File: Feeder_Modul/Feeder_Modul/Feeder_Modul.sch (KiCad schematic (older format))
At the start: 68 parts, among them J101 Conn_02x01, J102 Conn_01x06_Male, J103 Conn_02x01, J104 Conn_01x02_Male, J105 Conn_01x02_Male, J106 USB_A, J107 Conn_02x07_Odd_Even, Q101 BC847, SW101 SW_Push, SW102 SW_Push, SW103 SW_Push, SW104 SW_Push, SW105 SW_Push, U101 TPS560430, U102 STM32F105R8Tx, U103 SN65HVD230DR, U104 EE-SX1350_PCB, U105 DRV8835, Y101 48MHz

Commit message: PCB fast fertig geroutet, I2C EEPROM hinzugefügt
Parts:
- removed U103: SN65HVD230DR, Package_SO:SOIC-8_3.9x4.9mm_P1.27mm, symbol Interface_CAN_LIN:TJA1051T-3
- added C1: 100n 50V, Capacitor_SMD:C_0603_1608Metric, symbol Device:C_Small
- added C124, C2, C3: 10u 50V, Capacitor_SMD:C_1210_3225Metric, symbol Device:C_Small
- added D103, D104: LED_Blue, LED_SMD:LED_0603_1608Metric, symbol Device:LED_Small
- added J1, J108: Conn_02x01, Connector_PinHeader_2.54mm:PinHeader_1x02_P2.54mm_Vertical, symbol Connector_Generic:Conn_02x01
- added L1: 12u SRN4018, Inductor_SMD:L_Bourns-SRN4018, symbol Device:L_Small
- added R1, R2: 51K, Resistor_SMD:R_0603_1608Metric, symbol Device:R_Small
- added R123, R124, R126: 1k, Resistor_SMD:R_0603_1608Metric, symbol Device:R_Small
- added R125: DNP, Resistor_SMD:R_0603_1608Metric, symbol Device:R_Small
- added R127, R129: 10K, Resistor_SMD:R_0603_1608Metric, symbol Device:R_Small
- added R3: 22K1, Resistor_SMD:R_0603_1608Metric, symbol Device:R_Small
- added R4: 88K7, Resistor_SMD:R_0603_1608Metric, symbol Device:R_Small
- added U1: TPS560430, Package_TO_SOT_SMD:SOT-23-6, symbol PorjectLibrary:TPS560430
- added U103: M24C01-WMN, Package_SO:SOIC-8_3.9x4.9mm_P1.27mm, symbol Memory_EEPROM:M24C01-WMN
- added U107: SN65HVD230, Package_SO:SOIC-8_3.9x4.9mm_P1.27mm, symbol Interface_CAN_LIN:SN65HVD230
- C103: value 100n 50V -> 10u 50V; footprint Capacitor_SMD:C_0603_1608Metric -> Capacitor_SMD:C_1210_3225Metric; LCSC C282519 -> C1849
- C116, C119: value 100n -> 100n 50V; LCSC C83060 -> C282519
- C121: value 10u -> 10u 50V
- D101: value LED_Small -> LED_red; LCSC (none) -> C118330
- D102: value LED_Small -> LED_green; LCSC (none) -> C205443
- J101, J103: LCSC (none) -> C358684
- J104, J105: value Conn_01x02_Male -> Conn_02x01; LCSC (none) -> C358684
- J106: footprint Connector_USB:USB_A_CNCTech_1001-011-01101_Horizontal -> ProjectFootprints:USB-A-Conn_LCSC; symbol Connector:USB_A -> Feeder_Modul-rescue:USB_A-Connector; LCSC (none) -> C46405
- R108: value 10K -> 1k; LCSC C99198 -> C21190
- R109, R115, R121, R122: LCSC (none) -> C21190
- R113, R116, R117, R118, R119, R120: value 10k -> 10K; LCSC (none) -> C99198
- U102: LCSC (none) -> C80986
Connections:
- net labels added: ADDR0, ADDR1, ADDR2, ADDR3, ADDR4, ADDR5, ADDR6, ADDR7, I2C1_SCL, I2C1_SDA, PA5, PA6, PA7, PA8, PB12, PB13, PB14, PB15, PC4, PC5, PC6, PC7, PC8, PC9, TIM3_CH1, TIM3_CH2
- net labels removed: AD0, AD1, AD2, AD3, AD4, AD5, AD6, AD7, PA11, PA12, VBUS, VBUS_EN
- wire segments 218 -> 295
- no-connect marks 3 -> 29
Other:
- note added: "Address:\n0x50"
- note added: "Built in ESD Protection 16kV"
- note added: "High Speed Mode"
- note added: "Write enabled\n"
- note removed: "Replacement\nTJA1051T-3"
- moved on the sheet: C119, C121, J107, L102, R110, R111, R114

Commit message: Feeder fertig
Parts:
- added R128, R130, R131, R132, R133, R134, R135, R136: 88K7, Resistor_SMD:R_0603_1608Metric, symbol Device:R_Small
- R112: value 0R -> DNP
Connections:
- net +3V3: now also R128.2, R130.2, R131.2, R132.2, R133.2, R134.2, R135.2, R136.2
- net ADDR0: now also R128.1
- net ADDR1: now also R130.1
- net ADDR2: now also R131.1
- net ADDR3: now also R132.1
- net ADDR4: now also R133.1
- net ADDR5: now also R134.1
- net ADDR6: now also R135.1
- net ADDR7: now also R136.1
- net BTN_SBACK: now also U102.56 (PB4)
- net BTN_SFOR: now also U102.55 (PB3)
- net BTN_TBACK: now also U102.15 (PA1)
- net BTN_TFOR: now also U102.16 (PA2)
- net ENC_OUT: now also U102.30 (PB11)
- no-connect marks 29 -> 24
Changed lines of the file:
@@
 EESchema Schematic File Version 4
-EELAYER 30 0
+LIBS:Feeder_Modul-cache
+EELAYER 26 0
 EELAYER END
 $Descr A3 16535 11693
@@
 AR Path="/6057AAB9" Ref="R112"  Part="1"
 F 0 "R112" V 9600 1900 50  0000 R CNN
-F 1 "0R" V 9800 1850 50  0000 R CNN
+F 1 "DNP" V 9800 1900 50  0000 R CNN
 F 2 "Resistor_SMD:R_0603_1608Metric" H 9700 1850 50  0001 C CNN
 F 3 "~" H 9700 1850 50  0001 C CNN
@@
 NoConn ~ 5250 7650
 NoConn ~ 5250 7750
-NoConn ~ 5250 7850
-NoConn ~ 5250 7950
 NoConn ~ 5250 8050
 NoConn ~ 5250 8550
-NoConn ~ 5250 8650
 NoConn ~ 3850 8650
 NoConn ~ 3850 8750
@@
 NoConn ~ 3850 7350
 NoConn ~ 5250 5850
-NoConn ~ 5250 5950
-NoConn ~ 5250 6050
 NoConn ~ 5250 6150
 NoConn ~ 5250 6250
@@
 Wire Wire Line
 	2100 2500 2950 2500
+Text Label 14150 7300 2    50   ~ 0
+ADDR0
+Text Label 14150 7500 2    50   ~ 0
+ADDR2
+Text Label 14150 7700 2    50   ~ 0
+ADDR4
+Text Label 14150 7900 2    50   ~ 0
+ADDR6
+Text Label 14150 7400 2    50   ~ 0
+ADDR1
+Text Label 14150 7600 2    50   ~ 0
+ADDR3
+Text Label 14150 7800 2    50   ~ 0
+ADDR5
+Text Label 14150 8000 2    50   ~ 0
+ADDR7
+$Comp
+L Device:R_Small R128
+U 1 1 601C13DE
+P 14600 7300
+AR Path="/601C13DE" Ref="R128"  Part="1"
+AR Path="/5ED2496F/601C13DE" Ref="R?"  Part="1"
+AR Path="/5FDD0F66/601C13DE" Ref="R?"  Part="1"
+F 0 "R128" V 14650 7650 50  0000 C CNN
+F 1 "88K7" V 14650 7050 50  0000 C CNN
+F 2 "Resistor_SMD:R_0603_1608Metric" H 14600 7300 50  0001 C CNN
+F 3 "~" H 14600 7300 50  0001 C CNN
+F 4 "C163418" H 14600 7300 50  0001 C CNN "LCSC"
+	1    14600 7300
+	0    -1   -1   0
+$EndComp
+Wire Wire Line
+	14500 7300 14150 7300
+Wire Wire Line
+	14700 7300 15000 7300
+$Comp
+L Device:R_Small R130
+U 1 1 601F8F13
+P 14600 7400
+AR Path="/601F8F13" Ref="R130"  Part="1"
+AR Path="/5ED2496F/601F8F13" Ref="R?"  Part="1"
+AR Path="/5FDD0F66/601F8F13" Ref="R?"  Part="1"
+F 0 "R130" V 14650 7750 50  0000 C CNN
+F 1 "88K7" V 14650 7150 50  0000 C CNN
+F 2 "Resistor_SMD:R_0603_1608Metric" H 14600 7400 50  0001 C CNN
+F 3 "~" H 14600 7400 50  0001 C CNN
+F 4 "C163418" H 14600 7400 50  0001 C CNN "LCSC"
+	1    14600 7400
+	0    -1   -1   0
+$EndComp
+Wire Wire Line
+	14500 7400 14150 7400
+Wire Wire Line
+	14700 7400 15000 7400
+$Comp
+L Device:R_Small R131
+U 1 1 60214D10
+P 14600 7500
+AR Path="/60214D10" Ref="R131"  Part="1"
+AR Path="/5ED2496F/60214D10" Ref="R?"  Part="1"
+AR Path="/5FDD0F66/60214D10" Ref="R?"  Part="1"
+F 0 "R131" V 14650 7850 50  0000 C CNN
+F 1 "88K7" V 14650 7250 50  0000 C CNN
+F 2 "Resistor_SMD:R_0603_1608Metric" H 14600 7500 50  0001 C CNN
+F 3 "~" H 14600 7500 50  0001 C CNN
+F 4 "C163418" H 14600 7500 50  0001 C CNN "LCSC"
+	1    14600 7500
+	0    -1   -1   0
+$EndComp
+Wire Wire Line
+	14500 7500 14150 7500
+Wire Wire Line
+	14700 7500 15000 7500
+$Comp
+L Device:R_Small R132
+U 1 1 6023100C
+P 14600 7600
+AR Path="/6023100C" Ref="R132"  Part="1"
+AR Path="/5ED2496F/6023100C" Ref="R?"  Part="1"
+AR Path="/5FDD0F66/6023100C" Ref="R?"  Part="1"
+F 0 "R132" V 14650 7950 50  0000 C CNN
+F 1 "88K7" V 14650 7350 50  0000 C CNN
+F 2 "Resistor_SMD:R_0603_1608Metric" H 14600 7600 50  0001 C CNN
+F 3 "~" H 14600 7600 50  0001 C CNN
+F 4 "C163418" H 14600 7600 50  0001 C CNN "LCSC"
+	1    14600 7600
+	0    -1   -1   0
+$EndComp
+Wire Wire Line
+	14500 7600 14150 7600
+Wire Wire Line
+	14700 7600 15000 7600
+$Comp
+L Device:R_Small R133
+U 1 1 60231015
+P 14600 7700
+AR Path="/60231015" Ref="R133"  Part="1"
+AR Path="/5ED2496F/60231015" Ref="R?"  Part="1"
+AR Path="/5FDD0F66/60231015" Ref="R?"  Part="1"
+F 0 "R133" V 14650 8050 50  0000 C CNN
+F 1 "88K7" V 14650 7450 50  0000 C CNN
+F 2 "Resistor_SMD:R_0603_1608Metric" H 14600 7700 50  0001 C CNN
+F 3 "~" H 14600 7700 50  0001 C CNN
+F 4 "C163418" H 14600 7700 50  0001 C CNN "LCSC"
+	1    14600 7700
+	0    -1   -1   0
+$EndComp
+Wire Wire Line
+	14500 7700 14150 7700
+Wire Wire Line
+	14700 7700 15000 7700
+$Comp
+L Device:R_Small R134
+U 1 1 6023101E
+P 14600 7800
+AR Path="/6023101E" Ref="R134"  Part="1"
+AR Path="/5ED2496F/6023101E" Ref="R?"  Part="1"
+AR Path="/5FDD0F66/6023101E" Ref="R?"  Part="1"
+F 0 "R134" V 14650 8150 50  0000 C CNN
+F 1 "88K7" V 14650 7550 50  0000 C CNN
+F 2 "Resistor_SMD:R_0603_1608Metric" H 14600 7800 50  0001 C CNN
+F 3 "~" H 14600 7800 50  0001 C CNN
+F 4 "C163418" H 14600 7800 50  0001 C CNN "LCSC"
+	1    14600 7800
+	0    -1   -1   0
+$EndComp
+Wire Wire Line
+	14500 7800 14150 7800
+Wire Wire Line
+	14700 7800 15000 7800
+$Comp
+L Device:R_Small R135
+U 1 1 6024E2A7
+P 14600 7900
+AR Path="/6024E2A7" Ref="R135"  Part="1"
+AR Path="/5ED2496F/6024E2A7" Ref="R?"  Part="1"
+AR Path="/5FDD0F66/6024E2A7" Ref="R?"  Part="1"
+F 0 "R135" V 14650 8250 50  0000 C CNN
+F 1 "88K7" V 14650 7650 50  0000 C CNN
+F 2 "Resistor_SMD:R_0603_1608Metric" H 14600 7900 50  0001 C CNN
+F 3 "~" H 14600 7900 50  0001 C CNN
+F 4 "C163418" H 14600 7900 50  0001 C CNN "LCSC"
+	1    14600 7900
+	0    -1   -1   0
+$EndComp
+Wire Wire Line
+	14500 7900 14150 7900
+Wire Wire Line
+	14700 7900 15000 7900
+$Comp
+L Device:R_Small R136
+U 1 1 6024E2B0
+P 14600 8000
+AR Path="/6024E2B0" Ref="R136"  Part="1"
+AR Path="/5ED2496F/6024E2B0" Ref="R?"  Part="1"
+AR Path="/5FDD0F66/6024E2B0" Ref="R?"  Part="1"
+F 0 "R136" V 14650 8350 50  0000 C CNN
+F 1 "88K7" V 14650 7750 50  0000 C CNN
+F 2 "Resistor_SMD:R_0603_1608Metric" H 14600 8000 50  0001 C CNN
+F 3 "~" H 14600 8000 50  0001 C CNN
+F 4 "C163418" H 14600 8000 50  0001 C CNN "LCSC"
+	1    14600 8000
+	0    -1   -1   0
+$EndComp
+Wire Wire Line
+	14500 8000 14150 8000
+Wire Wire Line
+	14700 8000 15000 8000
+$Comp
+L power:+3V3 #PWR?
+U 1 1 6026BE8F
+P 15000 7200
+AR Path="/5FDD0F66/6026BE8F" Ref="#PWR?"  Part="1"
+AR Path="/6026BE8F" Ref="#PWR0158"  Part="1"
+F 0 "#PWR0158" H 15000 7050 50  0001 C CNN
+F 1 "+3V3" H 15015 7373 50  0000 C CNN
+F 2 "" H 15000 7200 50  0001 C CNN
+F 3 "" H 15000 7200 50  0001 C CNN
+	1    15000 7200
+	1    0    0    -1
+$EndComp
+Wire Wire Line
+	15000 8000 15000 7900
+Connection ~ 15000 7300
+Wire Wire Line
+	15000 7300 15000 7200
+Connection ~ 15000 7400
+Wire Wire Line
+	15000 7400 15000 7300
+Connection ~ 15000 7500
+Wire Wire Line
+	15000 7500 15000 7400
+Connection ~ 15000 7600
+Wire Wire Line
+	15000 7600 15000 7500
+Connection ~ 15000 7700
+Wire Wire Line
+	15000 7700 15000 7600
+Connection ~ 15000 7800
+Wire Wire Line
+	15000 7800 15000 7700
+Connection ~ 15000 7900
+Wire Wire Line
+	15000 7900 15000 7800
+Text Label 6050 5950 2    50   ~ 0
+BTN_TBACK
+Text Label 6050 6050 2    50   ~ 0
+BTN_TFOR
+Text Label 6150 7950 2    50   ~ 0
+BTN_SBACK
+Wire Wire Line
+	6150 7950 5250 7950
+Wire Wire Line
+	5250 7850 6150 7850
+Wire Wire Line
+	6050 5950 5250 5950
+Wire Wire Line
+	5250 6050 6050 6050
+Text Label 6150 7850 2    50   ~ 0
+BTN_SFOR
+Text Label 6150 8650 2    50   ~ 0
+ENC_OUT
+Wire Wire Line
+	6150 8650 5250 8650
 $EndSCHEMATC

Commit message: Feeder Microswitch für Tape Motor hinzugefügt. Einige 3D Step Modelle hinzugefügt. Stepper Board die Ecken abgerundet.
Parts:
- added J109: Conn_02x01, Connector_PinHeader_2.54mm:PinHeader_1x02_P2.54mm_Vertical, symbol Connector:Conn_01x02_Male
- added R137: 10K, Resistor_SMD:R_0603_1608Metric, symbol Device:R_Small
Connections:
- net +3V3: now also R137.2
- net GND: now also J109.2 (Pin_2)
- net LED_error: now also U102.51 (PC10); no longer U102.50 (PA15)
- net LED_status: now also U102.52 (PC11); no longer U102.51 (PC10)
- new net TAPE_MICROBTN: J109.1 (Pin_1), R137.1, U102.50 (PA15)
- no-connect marks 24 -> 23
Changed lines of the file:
@@
 EESchema Schematic File Version 4
-LIBS:Feeder_Modul-cache
-EELAYER 26 0
+EELAYER 30 0
 EELAYER END
 $Descr A3 16535 11693
@@
 NoConn ~ 5250 8050
 NoConn ~ 5250 8550
-NoConn ~ 3850 8650
 NoConn ~ 3850 8750
 NoConn ~ 3850 8850
@@
 	950  1450 650  1450
 Connection ~ 950  1450
-Text Label 6150 7350 2    50   ~ 0
-LED_error
 Text Label 3450 8550 2    50   ~ 0
+LED_error
+Text Label 3450 8650 2    50   ~ 0
 LED_status
 Wire Wire Line
@@
 Wire Wire Line
 	6150 8650 5250 8650
+$Comp
+L Connector:Conn_01x02_Male J109
+U 1 1 601775AC
+P 11950 4550
+F 0 "J109" H 11400 4550 50  0000 C CNN
+F 1 "Conn_02x01" H 11450 4450 50  0000 C CNN
+F 2 "Connector_PinHeader_2.54mm:PinHeader_1x02_P2.54mm_Vertical" H 11950 4550 50  0001 C CNN
+F 3 "~" H 11950 4550 50  0001 C CNN
+F 4 "C358684" H 11950 4550 50  0001 C CNN "LCSC"
+	1    11950 4550
+	1    0    0    -1
+$EndComp
+$Comp
+L Device:R_Small R137
+U 1 1 6017B811
+P 12150 4150
+F 0 "R137" H 12091 4104 50  0000 R CNN
+F 1 "10K" H 12091 4195 50  0000 R CNN
+F 2 "Resistor_SMD:R_0603_1608Metric" H 12150 4150 50  0001 C CNN
+F 3 "~" H 12150 4150 50  0001 C CNN
+F 4 "C99198" H 12150 4150 50  0001 C CNN "LCSC"
+	1    12150 4150
+	-1   0    0    1
+$EndComp
+$Comp
+L power:+3V3 #PWR0159
+U 1 1 6017C9DF
+P 12150 4050
+F 0 "#PWR0159" H 12150 3900 50  0001 C CNN
+F 1 "+3V3" H 12165 4223 50  0000 C CNN
+F 2 "" H 12150 4050 50  0001 C CNN
+F 3 "" H 12150 4050 50  0001 C CNN
+	1    12150 4050
+	1    0    0    -1
+$EndComp
+$Comp
+L power:GND #PWR0164
+U 1 1 6017D284
+P 12150 5000
+F 0 "#PWR0164" H 12150 4750 50  0001 C CNN
+F 1 "GND" H 12155 4827 50  0000 C CNN
+F 2 "" H 12150 5000 50  0001 C CNN
+F 3 "" H 12150 5000 50  0001 C CNN
+	1    12150 5000
+	1    0    0    -1
+$EndComp
+Wire Wire Line
+	12150 5000 12150 4650
+Wire Wire Line
+	12150 4550 12150 4300
+Text Label 12400 4300 0    50   ~ 0
+TAPE_MICROBTN
+Wire Wire Line
+	12400 4300 12150 4300
+Connection ~ 12150 4300
+Wire Wire Line
+	12150 4300 12150 4250
+Text Label 6150 7350 2    50   ~ 0
+TAPE_MICROBTN
+Wire Wire Line
+	3850 8650 3450 8650
 $EndSCHEMATC

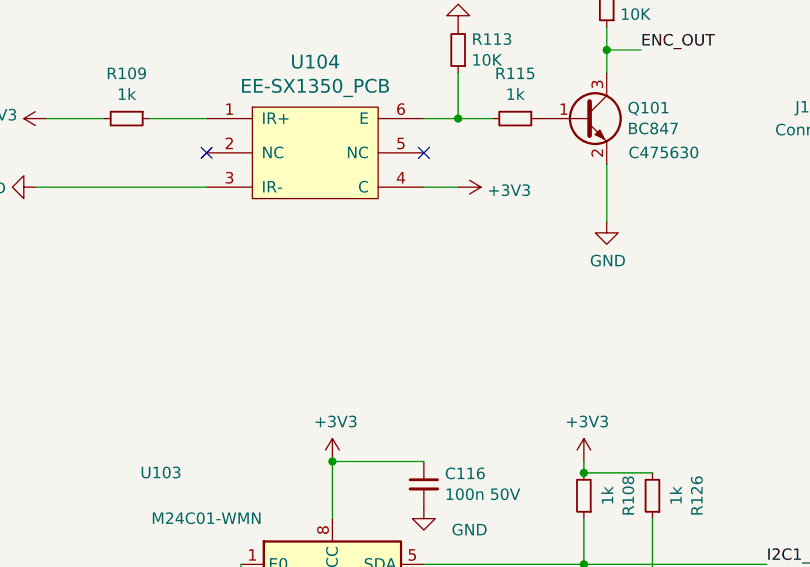
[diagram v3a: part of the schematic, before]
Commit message: Neue Lichtschranke für Feeder rausgesucht. TODO: neuer Footprint, Aljosha -> Update der CAD Daten
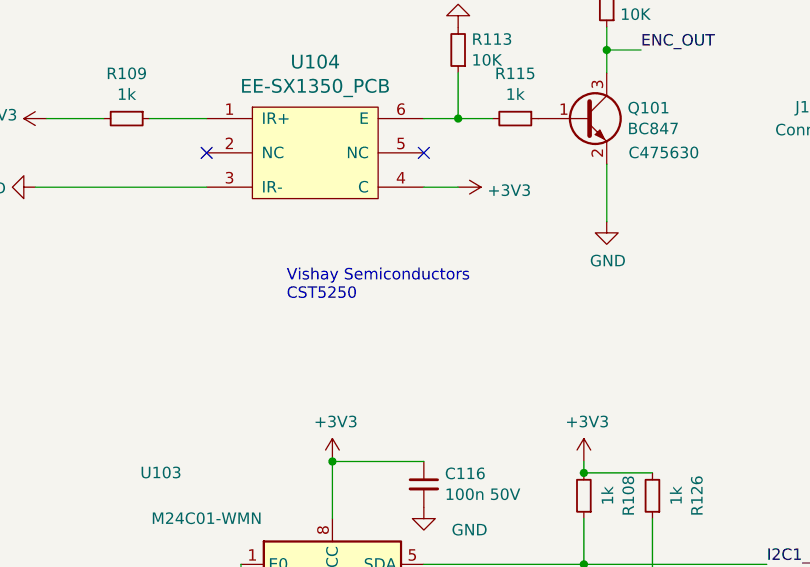
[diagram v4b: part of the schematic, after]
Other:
- note added: "Vishay Semiconductors\nCST5250"
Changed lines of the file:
@@
 Wire Wire Line
 	3850 8650 3450 8650
+Text Notes 9100 5400 0    50   ~ 0
+Vishay Semiconductors\nCST5250
 $EndSCHEMATC
